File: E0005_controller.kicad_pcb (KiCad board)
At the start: 4 copper layers, 125 x 65 mm, 270 parts, among them J1 SM04B-GHS-TB, J10 FH12-18S-0.5SH, J11 USB4105-GF-A, J12 SM02B-GHS-TB, J2 SM04B-GHS-TB, J3 SM04B-GHS-TB, J4 SM04B-GHS-TB, J5 SM06B-GHS-TB, J6 SM02B-GHS-TB, J7 SM02B-GHS-TB, J8 SM02B-GHS-TB, J9 SM02B-GHS-TB, Q1 PSMN2R0-30YLDX, Q11 2N7002, Q12 2N7002, Q13 AO3401A, Q14 2N7002, Q2 PSMN2R0-30YLDX, Q3 2N7002, Q4 2N7002, Q5 2N7002, Q6 2N7002, Q7 2N7002, SW1 PWR, SW2 BOOT, SW3 RESET, U1 ESP32-S3-WROOM-1-N16R2, U10 TPS259470ARPW, U11 TPS259470ARPW, U12 TPS259470ARPW, U13 TPS259470ARPW, U14 TPS259470ARPW, U15 MAX17205G+, U16 TPS259470ARPW, U17 TPS56637RPAR, U2 BQ25887RGER, U4 USBLC6-2SC6, U5 TPS629210DRL, U6 S-8252AAG-M6T1U, U8 PCA9548APW, U9 TCA9535PWR

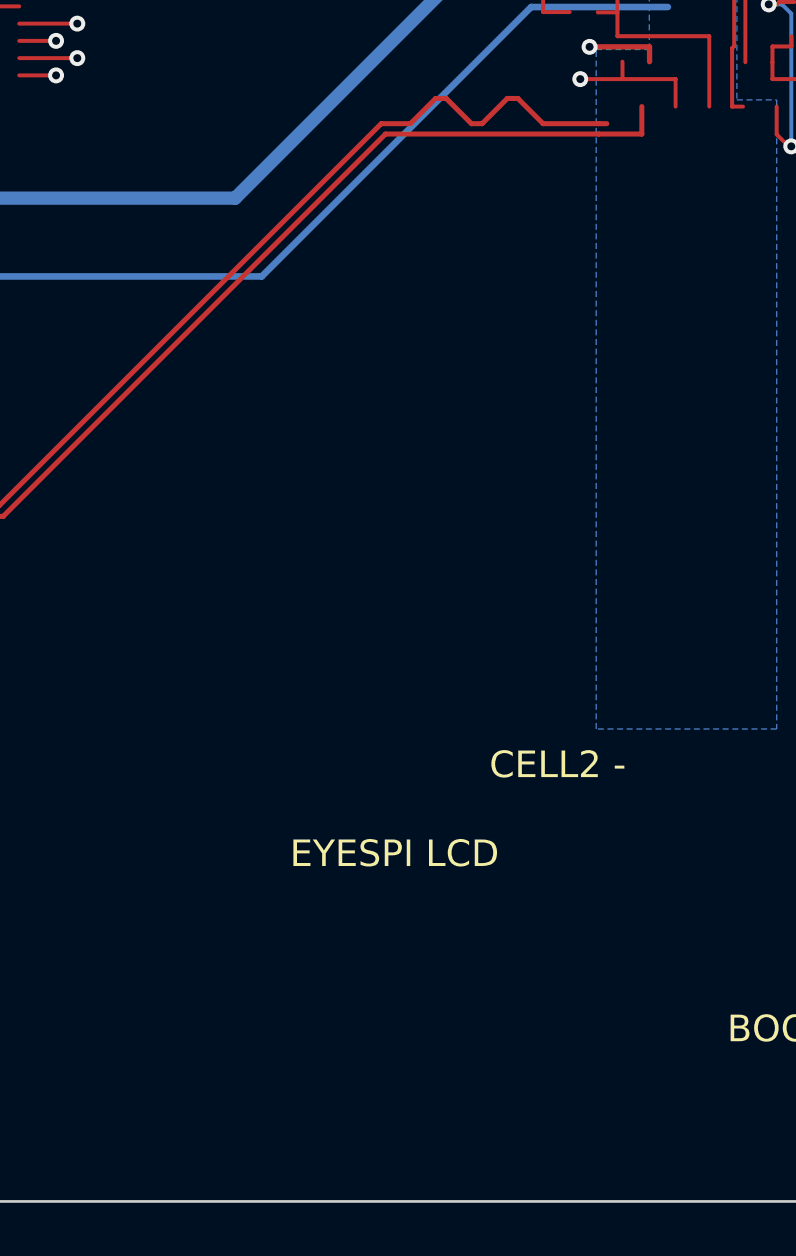
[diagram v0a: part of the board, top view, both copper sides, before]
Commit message: E0005 routing: U1 west column, LCD J10 via comb + F/B LCD bus (MOSI/SCK/MISO/DC/LITE/CS/TSCS), J10 pull-ups
Co-Authored-By: Claude Opus 5.5 <noreply@anthropic.com>
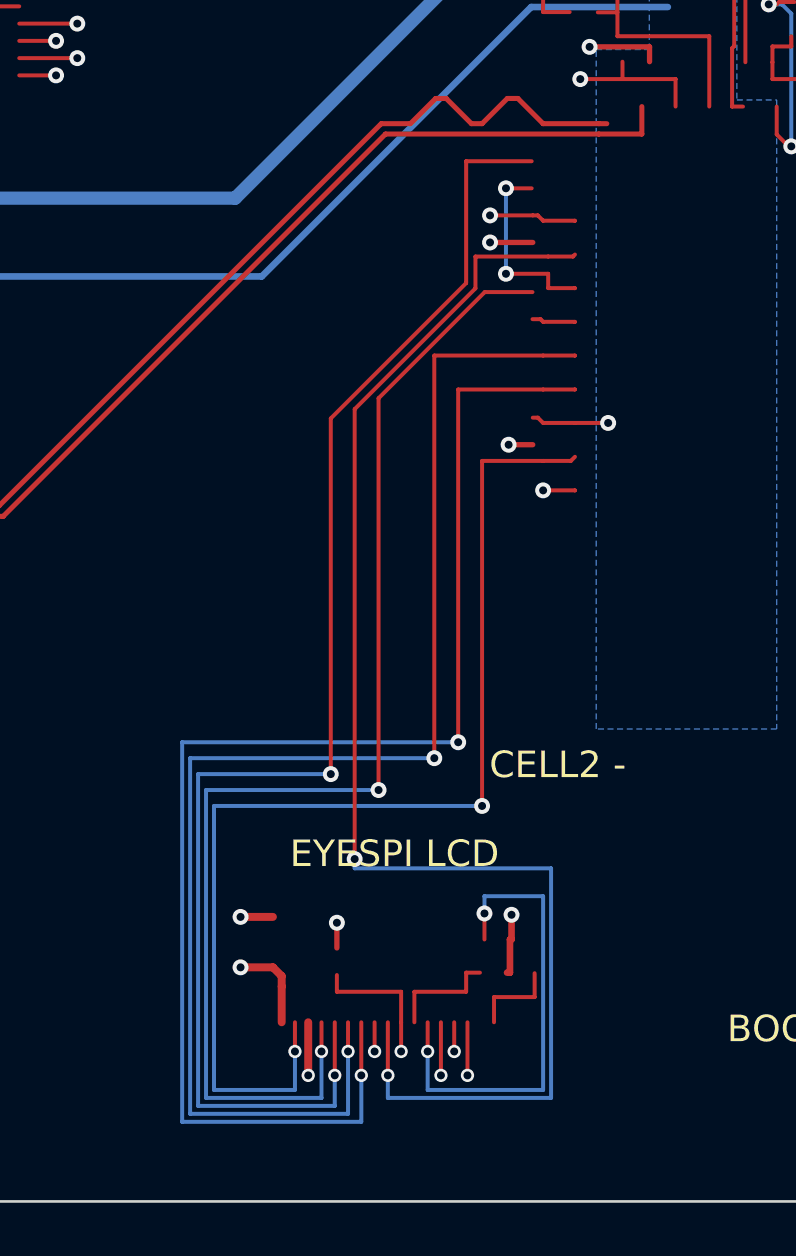
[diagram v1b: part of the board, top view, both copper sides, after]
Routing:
- net /MCU, UI, LCD, switches/LCD_CS: track 0.00 -> 53.8 mm, vias 0 -> 2
- net /MCU, UI, LCD, switches/LCD_MOSI: track 0.00 -> 53.5 mm, vias 0 -> 2
- net /MCU, UI, LCD, switches/LCD_DC: track 0.00 -> 52.9 mm, vias 0 -> 2
- net /MCU, UI, LCD, switches/LCD_MISO: track 0.00 -> 52.5 mm, vias 0 -> 2
- net /MCU, UI, LCD, switches/LCD_SCK: track 0.00 -> 47.5 mm, vias 0 -> 2
- net /MCU, UI, LCD, switches/LCD_LITE: track 0.00 -> 43.0 mm, vias 0 -> 2
- net /MCU, UI, LCD, switches/LCD_TSCS: track 0.00 -> 18.0 mm, vias 0 -> 2
- net +3V3: track 113.8 -> 123.1 mm, vias 33 -> 38
- net /MCU, UI, LCD, switches/LCD_MOSI_MCU: track 0.00 -> 7.33 mm, vias 0 -> 2
- net /MCU, UI, LCD, switches/LCD_SDCS: track 0.00 -> 5.30 mm, vias 0 -> 1
- net /MCU, UI, LCD, switches/LCD_MEMCS: track 0.00 -> 4.34 mm
- net /MCU, UI, LCD, switches/EYESPI_GP1: track 0.00 -> 3.38 mm
- net I2C0_SCL: track 9.49 -> 12.8 mm, vias 1 -> 2
- net GND: track 160.3 -> 163.5 mm, vias 115 -> 117
- net /MCU, UI, LCD, switches/PWR_BTN_N: track 0.00 -> 2.93 mm, vias 0 -> 1
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
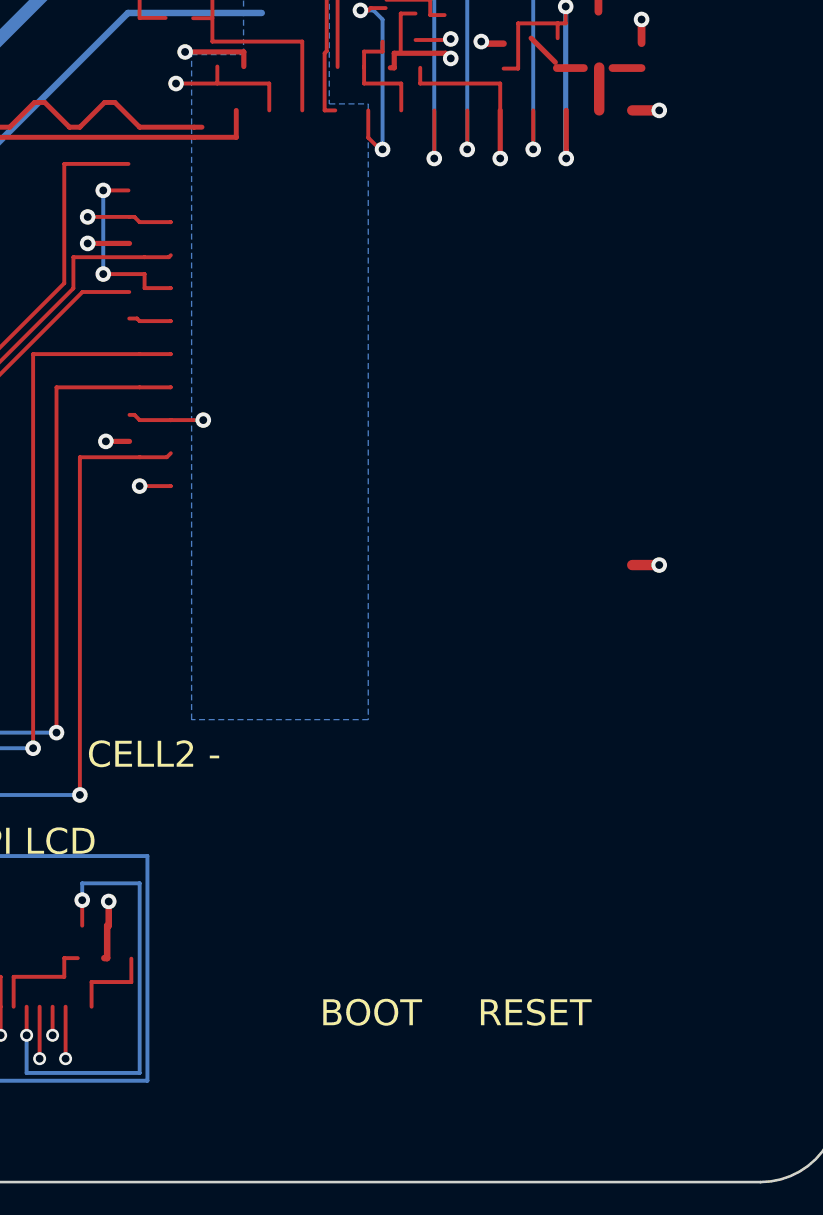
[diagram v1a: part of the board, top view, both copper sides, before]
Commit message: E0005 routing: U1 south row (BOOT/EN switches, LED, pull-ups, In2 starts of west-going lines), LCD RST/SDCS/TOUCH In2 to J10 comb
Co-Authored-By: Claude Opus 5.5 <noreply@anthropic.com>
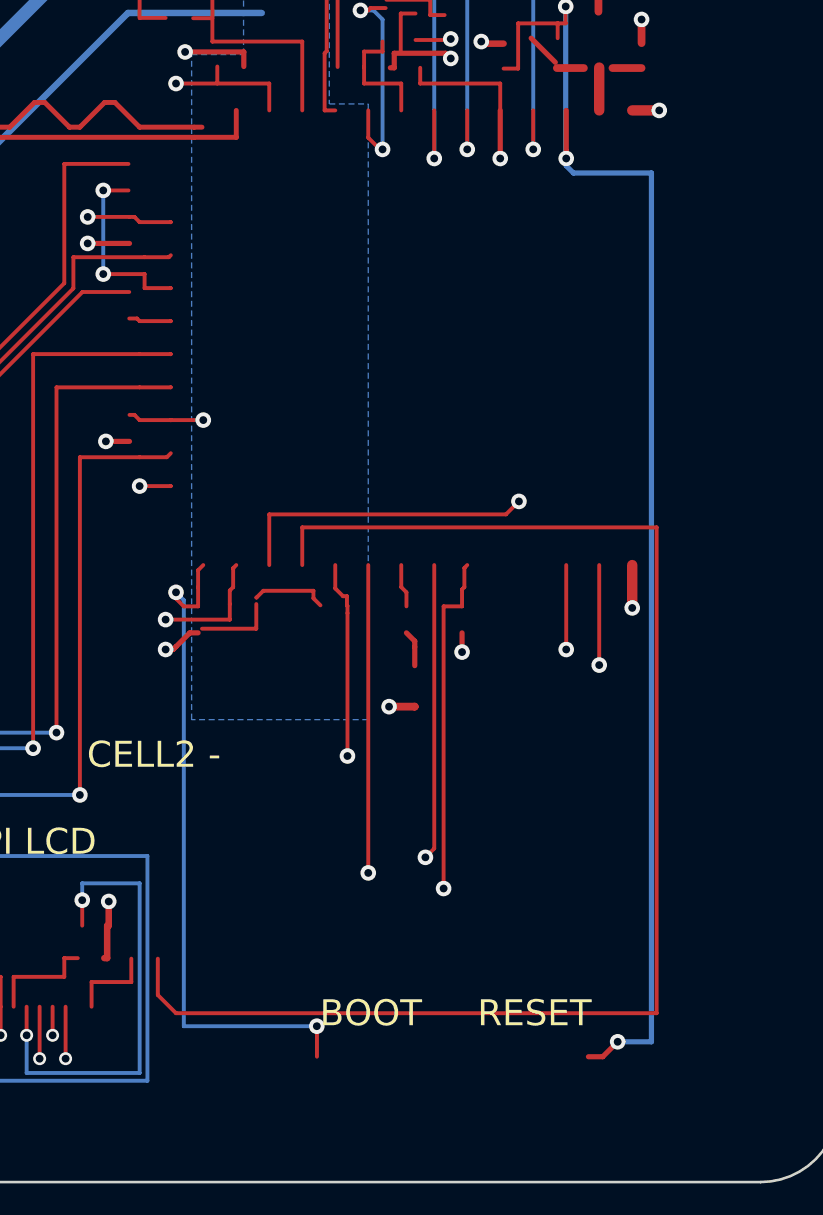
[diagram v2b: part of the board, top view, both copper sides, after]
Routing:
- net /MCU, UI, LCD, switches/SPARE37: track 0.00 -> 54.7 mm
- net CHG_INT_N: track 10.9 -> 54.5 mm
- net PWR_HOLD: track 4.26 -> 47.8 mm, vias 1 -> 2
- net /MCU, UI, LCD, switches/EN: track 13.1 -> 52.8 mm, vias 2 -> 3
- net /MCU, UI, LCD, switches/LCD_SDCS: track 5.30 -> 39.9 mm, vias 1 -> 2
- net /MCU, UI, LCD, switches/TOUCH_INT_N: track 2.00 -> 36.3 mm, vias 1 -> 2
- net I2C1_SDA: track 2.23 -> 36.1 mm, vias 2 -> 3
- net /MCU, UI, LCD, switches/LCD_RST: track 1.10 -> 34.3 mm, vias 1 -> 2
- net I2C1_SCL: track 2.31 -> 34.2 mm, vias 1 -> 2
- net /MCU, UI, LCD, switches/BOOT: track 0.00 -> 26.0 mm, vias 0 -> 2
- net LCD_SDA: track 2.51 -> 24.0 mm
- net MUX_RST_N: track 2.31 -> 22.7 mm, vias 1 -> 2
- net LCD_SCL: track 8.38 -> 27.6 mm
- net +3V3: track 123.1 -> 131.3 mm, vias 38 -> 40
- net GAUGE_ALRT_N: track 0.00 -> 7.27 mm, vias 0 -> 1
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
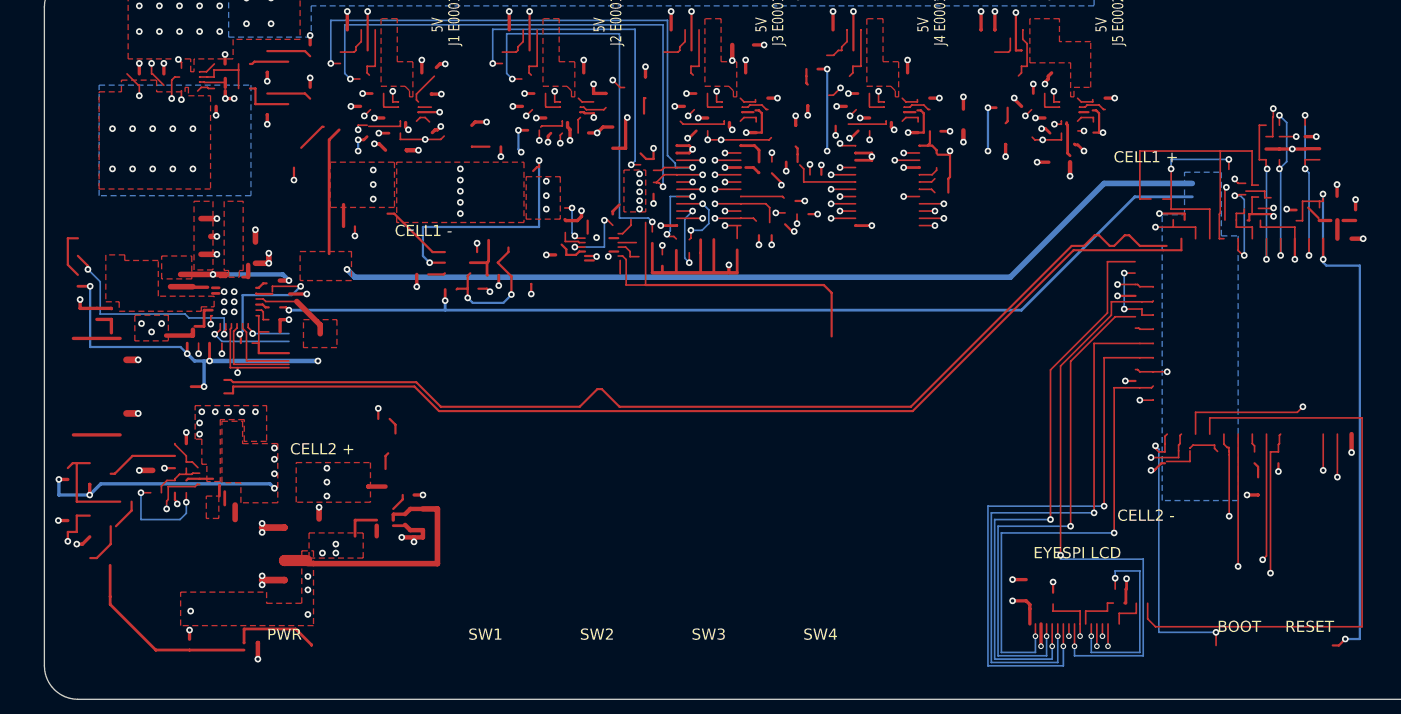
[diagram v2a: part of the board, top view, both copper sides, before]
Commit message: E0005 routing: west-going long lines from U1 (GAUGE_ALRT_N, CHG_INT_N, PWR_HOLD, PWR_BTN_N; MUX_RST/I2C1 partial), eFuse split-pin and switch twin-pad links
Co-Authored-By: Claude Opus 5.5 <noreply@anthropic.com>
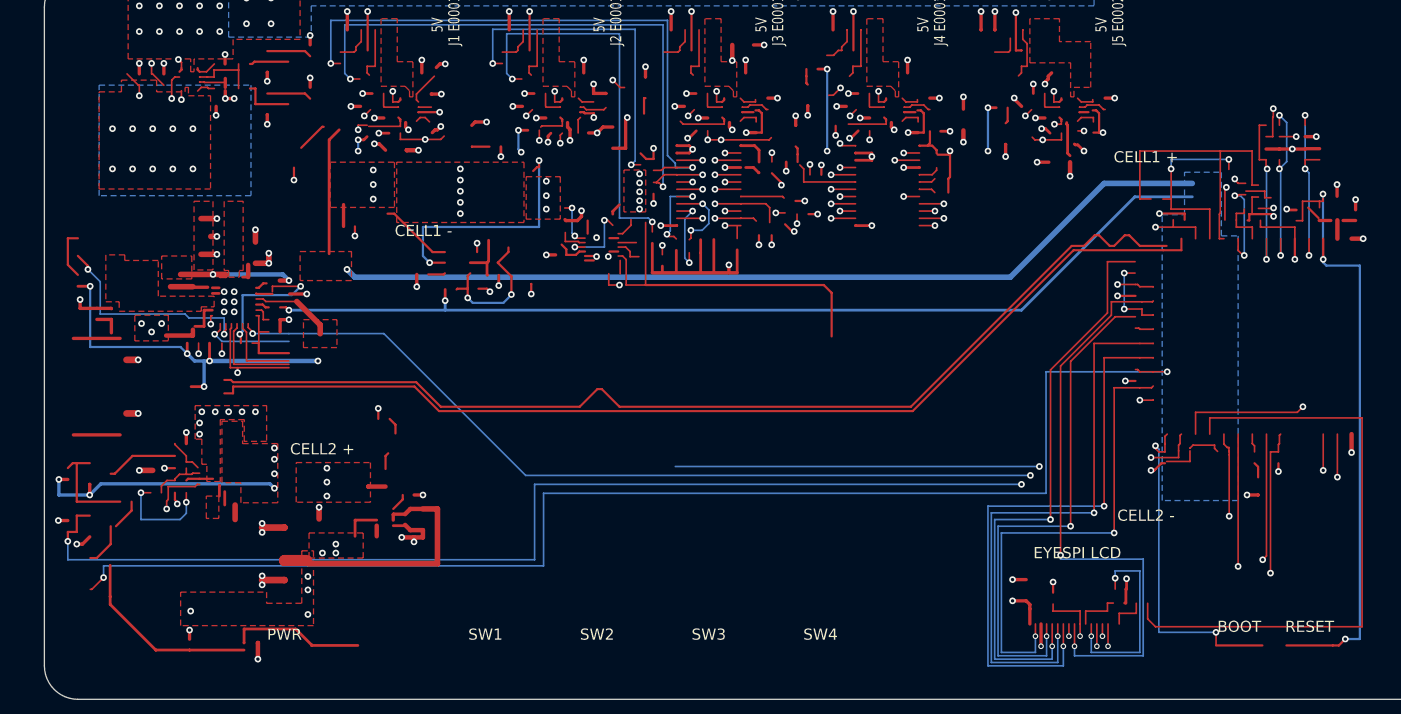
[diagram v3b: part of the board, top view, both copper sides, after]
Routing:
- net /MCU, UI, LCD, switches/PWR_BTN_N: track 2.93 -> 118.2 mm, vias 1 -> 2
- net PWR_HOLD: track 47.8 -> 150.5 mm, vias 2 -> 3
- net CHG_INT_N: track 54.5 -> 134.9 mm, vias 2 -> 3
- net GAUGE_ALRT_N: track 7.27 -> 69.7 mm, vias 1 -> 2
- net MUX_RST_N: track 22.7 -> 64.0 mm, vias 2 -> 3
- net I2C1_SDA: track 36.1 -> 66.9 mm
- net I2C1_SCL: track 34.2 -> 59.3 mm
- net /MCU, UI, LCD, switches/PB_RAW: track 25.1 -> 29.3 mm
- net /MCU, UI, LCD, switches/EN: track 52.8 -> 57.0 mm
- net /MCU, UI, LCD, switches/BOOT: track 26.0 -> 30.2 mm

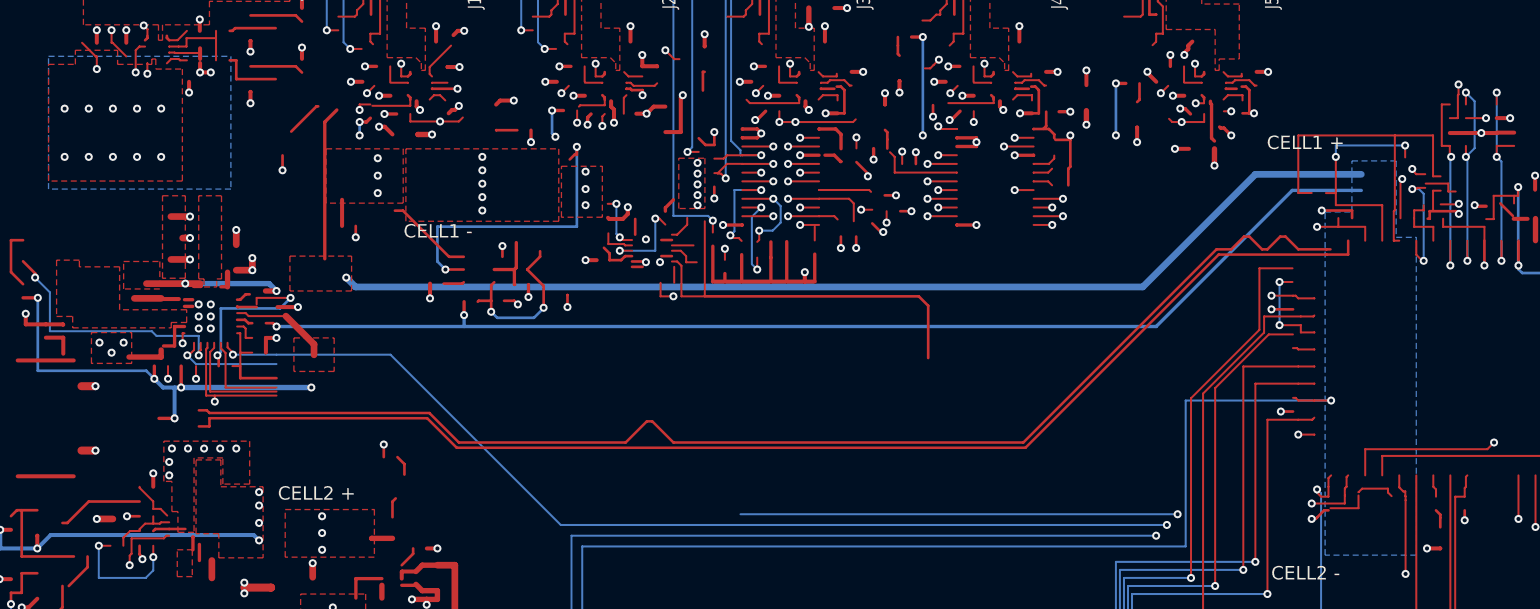
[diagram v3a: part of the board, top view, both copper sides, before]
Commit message: E0005 routing: CC1/CC2 from the U1 sense dividers to the USB-C resistors; CHG_INT_N In2 hop
Co-Authored-By: Claude Opus 5.5 <noreply@anthropic.com>
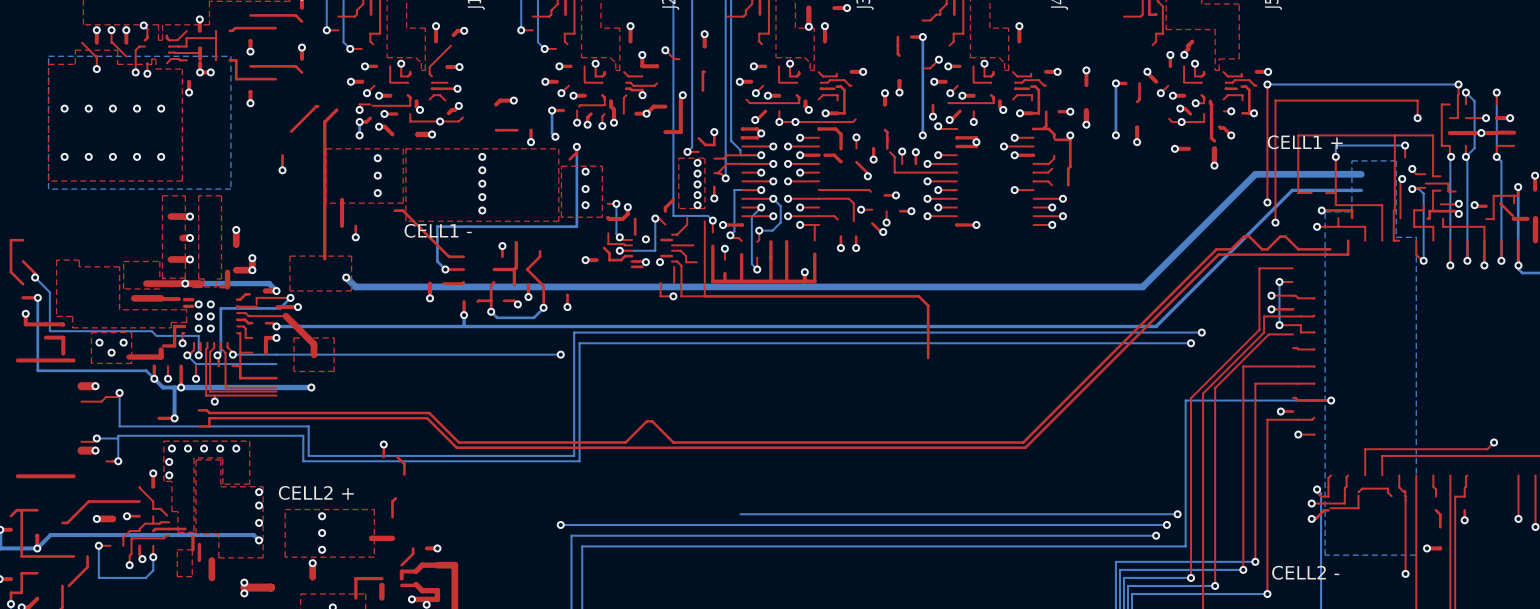
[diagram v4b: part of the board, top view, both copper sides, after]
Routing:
- net /Power: USB-C, U_IN, charger, 5 V buck, 3V3/CC1: track 1.50 -> 139.2 mm, vias 1 -> 5
- net /Power: USB-C, U_IN, charger, 5 V buck, 3V3/CC2: track 3.13 -> 138.7 mm, vias 1 -> 6
- net CHG_INT_N: track 134.9 -> 142.3 mm, vias 3 -> 5

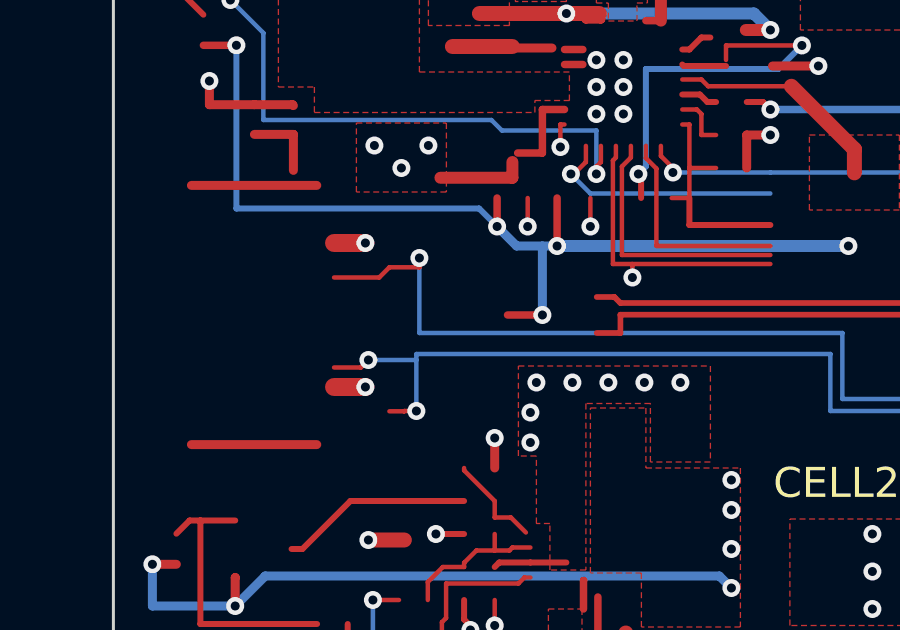
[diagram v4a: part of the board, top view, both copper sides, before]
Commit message: E0005 routing: USB-C side D+/D- (J11 -> U4 ESD -> R2/R3, B-row pins tied with 0.45 vias)
Co-Authored-By: Claude Opus 5.5 <noreply@anthropic.com>
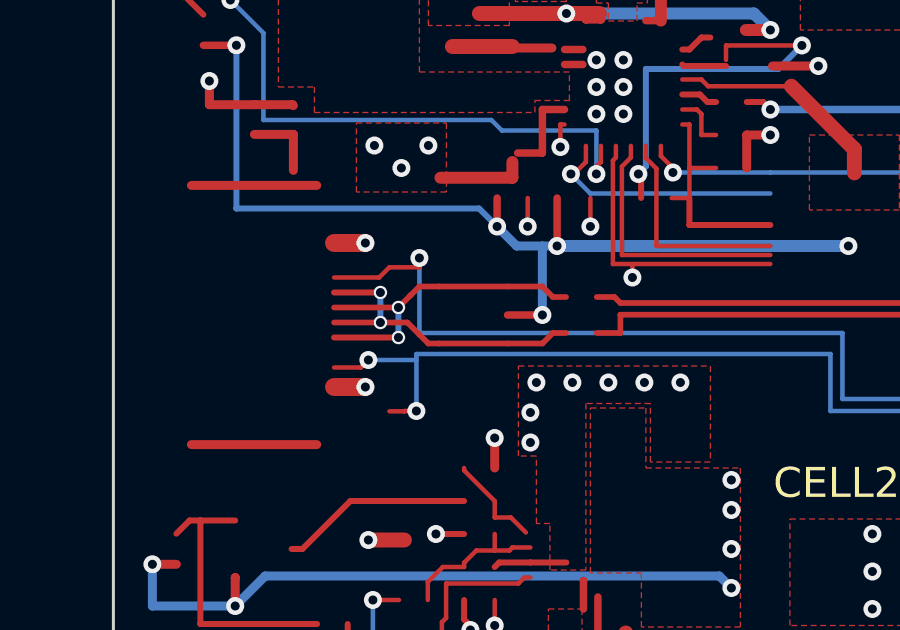
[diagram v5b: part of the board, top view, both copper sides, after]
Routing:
- net /Power: USB-C, U_IN, charger, 5 V buck, 3V3/USB_DP_C: track 0.00 -> 11.3 mm, vias 0 -> 2
- net /Power: USB-C, U_IN, charger, 5 V buck, 3V3/USB_DN_C: track 0.00 -> 10.7 mm, vias 0 -> 2
